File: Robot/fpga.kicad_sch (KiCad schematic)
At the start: 2 parts, among them U2 ICE40UP5K-SG48ITR, U3 74HCT245

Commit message: Update Robot SCH
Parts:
- added C1, C2: C, symbol Device:C
- added R1, R2, R3, R4: R, symbol Device:R
- added U4: DRV8845RHHR, symbol local:DRV8845
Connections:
- net GND: now also R1.1, R2.1, R3.1, R4.1, U4.16 (GND), U4.30 (PGND), U4.49 (PAD); no longer U3.13 (B5)
- net PWR_OFF: now also U2.10 (IOB_18a); no longer U2.42 (IOT_51a)
- net at U2.35 (IOT_46b_G0): now also U3.18 (B0); no longer U3.17 (B1)
- net at U2.36 (IOT_48b): now also U3.17 (B1); no longer U3.16 (B2)
- net at U2.37 (IOT_45a_G1): now also U4.11 (~{SLEEP}); no longer U3.18 (B0)
- net at U2.38 (IOT_50b): now also U3.15 (B3); no longer U3.14 (B4)
- net at U2.43 (IOT_49a): now also U3.16 (B2); no longer U3.15 (B3)
- net at U2.11 (IOB_20a): now also U3.13 (B5)
- net DLED: now reaches U3.7 (A5)
- net DRV_DIR1: no longer names the net of U2.25 (IOT_36b)
- net DRV_DIR1: now also U4.29 (I11), U4.34 (I01)
- net DRV_DIR2: no longer names the net of U2.23 (IOT_37a)
- net DRV_DIR2: now also U4.18 (PHASE1)
- net DRV_DIR3: no longer names the net of U2.27 (IOT_38b)
- net DRV_DIR3: now also U4.28 (I12), U4.35 (I02)
- net DRV_DIR4: no longer names the net of U2.26 (IOT_39a)
- net DRV_DIR4: now also U4.17 (PHASE2)
- net DRV_EN1: no longer names the net of U2.28 (IOT_41a)
- net DRV_EN1: now also U4.27 (I13), U4.36 (I03)
- net DRV_EN2: no longer names the net of U2.31 (IOT_42b)
- net DRV_EN2: now also U4.10 (PHASE3)
- net DRV_EN3: no longer names the net of U2.32 (IOT_43a)
- net DRV_EN3: now also U4.1 (I04), U4.19 (I14)
- net DRV_EN4: no longer names the net of U2.34 (IOT_44b)
- net DRV_EN4: now also U4.9 (PHASE4)
- new net: R2.2, U4.7 (SENSE2)
- new net: R1.2, U4.3 (SENSE1)
- new net: C2.1, U4.31 (VCP)
- new net: R4.2, U4.21 (SENSE4)
- new net: U2.42 (IOT_51a), U3.14 (B4)
- new net: R3.2, U4.25 (SENSE3)
- new net: C1.1, U4.32 (CP1)
- new net: C1.2, U4.33 (CP2)
- new net +12V: C2.2, U4.23 (VM2), U4.5 (VM1)
- new net VREF: U4.12 (VREF1), U4.13 (VREF2), U4.14 (VREF3), U4.15 (VREF4)
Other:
- moved on the sheet: U2A, U3

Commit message: Updated Robot SCH
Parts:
- removed unit 4 of U2
- added C3, C7, C8, C9: 1.0, symbol Device:C
- added C4, C5: 10n, symbol Device:C
- added C6: C_Polarized, symbol Device:C_Polarized
- added CN1, CN2, CN3, CN4: BM04B-SRSS-TB, easyeda2kicad:CONN-SMD_BM04B-SRSS-TB, symbol easyeda2kicad:BM04B-SRSS-TB
- added D1, D2, D3: KT-0603R, LED_SMD:LED_0603_1608Metric, symbol Device:LED
- added J3, J4, J5, J6: Motor, symbol Connector:Conn_01x02_Pin
- added R10, R11, R12, R13, R6, R7, R8, R9: NP, symbol Device:R
- added R14, R15, R16: R, symbol Device:R
- added SW2: User, symbol Switch:SW_Push
- C1: value C -> 22n
- C2: value C -> 0.22
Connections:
- net +12V: now also C4.2, C5.2, C6.1
- net +5V: now also C3.2
- net DLED: now also U3.9 (A7); no longer U3.7 (A5)
- net GND: now also U4.37 (PAD), C3.1, C4.1, C5.1, C6.2, C7.2, C8.2, C9.1, CN1.0, CN1.1, CN2.0, CN2.1, CN3.0, CN3.1, CN4.0, CN4.1, SW2.1; no longer U3.11 (B7), U3.12 (B6), U4.49 (PAD)
- net +3.3V: now reaches U2.33 (VCCIO_0)
- net +3.3V: now also U2.1 (VCCIO_2), U2.22 (SPI_VCCIO1), C7.1, C8.1, C9.2, CN1.4, CN2.4, CN3.4, CN4.4, R10.2, R11.2, R12.2, R13.2, R14.1, R15.1, R16.1, R6.2, R7.2, R8.2, R9.2
- net at U4.2 (OUT1A): now also J3.1 (Pin_1)
- net at U4.20 (OUT4A): now also J6.1 (Pin_1)
- net at U4.22 (OUT4B): now also J6.2 (Pin_2)
- net at U4.24 (OUT3B): now also J5.2 (Pin_2)
- net at U4.26 (OUT3A): now also J5.1 (Pin_1)
- net at U4.4 (OUT1B): now also J3.2 (Pin_2)
- net at U4.6 (OUT2B): now also J4.2 (Pin_2)
- net at U4.8 (OUT2A): now also J4.1 (Pin_1)
- net at U2.12 (IOB_22a): now also U3.12 (B6)
- net PwrBtnInput: now reaches U2.13 (IOB_24a)
- net at U2.20 (IOB_25b_G3): now also SW2.2
- net at U2.21 (IOB_23b): now also U3.11 (B7)
- net SERV7: now reaches U3.8 (A6)
- net DRV_QENCA1: no longer names the net of U2.46 (IOB_0a)
- net DRV_QENCA1: now also CN1.2, R11.1
- net DRV_QENCA2: no longer names the net of U2.47 (IOB_2a)
- net DRV_QENCA2: now also CN1.3, R10.1
- net DRV_QENCA3: no longer names the net of U2.44 (IOB_3b_G6)
- net DRV_QENCA3: now also CN2.2, R13.1
- net DRV_QENCA4: no longer names the net of U2.48 (IOB_4a)
- net DRV_QENCA4: now also CN2.3, R12.1
- net DRV_QENCB1: no longer names the net of U2.45 (IOB_5b)
- net DRV_QENCB1: now also CN3.2, R9.1
- net DRV_QENCB2: no longer names the net of U2.2 (IOB_6a)
- net DRV_QENCB2: now also CN3.3, R8.1
- net DRV_QENCB3: no longer names the net of U2.4 (IOB_8a)
- net DRV_QENCB3: now also CN4.2, R6.1
- net DRV_QENCB4: no longer names the net of U2.3 (IOB_9b)
- net DRV_QENCB4: now also CN4.3, R7.1
- net LED1: no longer names the net of U2.39 (RGB0)
- net LED1: now also D2.1 (K)
- net LED2: no longer names the net of U2.40 (RGB1)
- net LED2: now also D1.1 (K)
- net LED3: no longer names the net of U2.41 (RGB2)
- net LED3: now also D3.1 (K)
- net VREF renamed VREF ?
- new net: D2.2 (A), R14.2
- new net: D1.2 (A), R15.2
- new net: D3.2 (A), R16.2
- new net SERV6: U3.7 (A5)
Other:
- note added: "GND C1 C2 VCC"
- moved on the sheet: U2A, U2C

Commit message: Updated Robot SCH
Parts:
- removed CN1, CN2, CN3, CN4: BM04B-SRSS-TB, easyeda2kicad:CONN-SMD_BM04B-SRSS-TB, symbol easyeda2kicad:BM04B-SRSS-TB
- removed J3, J4, J5, J6: Motor, symbol Connector:Conn_01x02_Pin
- added C52: 1.0, symbol Device:C
- added J16: M1, symbol local:Motor
- added J17: M2, symbol local:Motor
- added J18: M3, symbol local:Motor
- added J19: M4, symbol local:Motor
- added R48, R49, R50, R51, R52, R53, R54, R55: 10K, symbol Device:R
- added U16: MCP4728, Package_SO:MSOP-10_3x3mm_P0.5mm, symbol Analog_DAC:MCP4728
- C6: value C_Polarized -> 470x16V
- R1, R2, R3, R4: value R -> FRM252WJR220TK (0.22); MPN (none) -> C7420023
- R14, R15, R16: value R -> ~
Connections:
- net +3.3V: now also C52.2, J16.2 (Vcc), J17.2 (Vcc), J18.2 (Vcc), J19.2 (Vcc), U16.1 (VDD)
- net GND: now also C52.1, J16.5 (GND), J17.5 (GND), J18.5 (GND), J19.5 (GND), R52.2, R53.2, R54.2, R55.2, U16.10 (VSS), U16.4 (~{LDAC})
- net SCL: now also U16.2 (SCL)
- net SDA: now also U16.3 (SDA)
- net at R11.1, U2.46 (IOB_0a): now also J16.4 (C1)
- net at R13.1, U2.44 (IOB_3b_G6): now also J17.4 (C1)
- net at R12.1, U2.48 (IOB_4a): now also J17.3 (C2)
- net at R8.1: now also U2.3 (IOB_9b), J19.3 (C2); no longer U2.2 (IOB_6a)
- net at R9.1: now also U2.4 (IOB_8a), J19.4 (C1); no longer U2.45 (IOB_5b)
- net at U4.8 (OUT2A): now also J17.6 (M+)
- net at U4.6 (OUT2B): now also J17.1 (M-)
- net at U4.26 (OUT3A): now also J18.6 (M+)
- net at U4.24 (OUT3B): now also J18.1 (M-)
- net at R6.1: now also U2.2 (IOB_6a), J18.3 (C2); no longer U2.4 (IOB_8a)
- net at R7.1: now also U2.45 (IOB_5b), J18.4 (C1); no longer U2.3 (IOB_9b)
- net at U4.2 (OUT1A): now also J16.6 (M+)
- net at U4.4 (OUT1B): now also J16.1 (M-)
- net at R10.1, U2.47 (IOB_2a): now also J16.3 (C2)
- net at U4.20 (OUT4A): now also J19.6 (M+)
- net at U4.22 (OUT4B): now also J19.1 (M-)
- removed net VREF ?: U4.12 (VREF1), U4.13 (VREF2), U4.14 (VREF3), U4.15 (VREF4)
- new net: R48.1, U16.6 (VOUTA)
- new net: R49.1, U16.7 (VOUTB)
- new net: R50.1, U16.8 (VOUTC)
- new net: R51.1, U16.9 (VOUTD)
- new net VREF1: R48.2, R52.1, U4.12 (VREF1)
- new net VREF2: R49.2, R53.1, U4.13 (VREF2)
- new net VREF3: R50.2, R54.1, U4.14 (VREF3)
- new net VREF4: R51.2, R55.1, U4.15 (VREF4)
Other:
- note removed: "GND C1 C2 VCC"

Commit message: Started PCB roughting
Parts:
- C10: renamed from C9; footprint (none) -> Capacitor_SMD:C_0603_1608Metric_Pad1.08x0.95mm_HandSolder
- C11: renamed from C52; footprint (none) -> Capacitor_SMD:C_0603_1608Metric_Pad1.08x0.95mm_HandSolder
- C2: renamed from C8; footprint (none) -> Capacitor_SMD:C_0603_1608Metric_Pad1.08x0.95mm_HandSolder
- C3: renamed from C6; footprint (none) -> Capacitor_THT:CP_Radial_D8.0mm_P3.80mm
- C4, C5: footprint (none) -> Capacitor_SMD:C_0603_1608Metric_Pad1.08x0.95mm_HandSolder
- C6: renamed from C1; footprint (none) -> Capacitor_SMD:C_0603_1608Metric_Pad1.08x0.95mm_HandSolder
- C7: renamed from C2; footprint (none) -> Capacitor_SMD:C_0603_1608Metric_Pad1.08x0.95mm_HandSolder
- C8: renamed from C7; footprint (none) -> Capacitor_SMD:C_0603_1608Metric_Pad1.08x0.95mm_HandSolder
- C9: renamed from C3; footprint (none) -> Capacitor_SMD:C_0603_1608Metric_Pad1.08x0.95mm_HandSolder
- J12: renamed from J16; footprint (none) -> easyeda2kicad:CONN-TH_S6B-XH-A-1-LF-SN
- J13: renamed from J17; footprint (none) -> easyeda2kicad:CONN-TH_S6B-XH-A-1-LF-SN
- J14: renamed from J18; footprint (none) -> easyeda2kicad:CONN-TH_S6B-XH-A-1-LF-SN
- J15: renamed from J19; footprint (none) -> easyeda2kicad:CONN-TH_S6B-XH-A-1-LF-SN
- R10: renamed from R16; footprint (none) -> Resistor_SMD:R_0603_1608Metric_Pad0.98x0.95mm_HandSolder
- R11: renamed from R12; footprint (none) -> Resistor_SMD:R_0603_1608Metric_Pad0.98x0.95mm_HandSolder
- R12: renamed from R13; footprint (none) -> Resistor_SMD:R_0603_1608Metric_Pad0.98x0.95mm_HandSolder
- R13: renamed from R10; footprint (none) -> Resistor_SMD:R_0603_1608Metric_Pad0.98x0.95mm_HandSolder
- R14: renamed from R11; footprint (none) -> Resistor_SMD:R_0603_1608Metric_Pad0.98x0.95mm_HandSolder
- R15: renamed from R7; footprint (none) -> Resistor_SMD:R_0603_1608Metric_Pad0.98x0.95mm_HandSolder
- R16: renamed from R6; footprint (none) -> Resistor_SMD:R_0603_1608Metric_Pad0.98x0.95mm_HandSolder
- R17: renamed from R9; footprint (none) -> Resistor_SMD:R_0603_1608Metric_Pad0.98x0.95mm_HandSolder
- R18: renamed from R8; footprint (none) -> Resistor_SMD:R_0603_1608Metric_Pad0.98x0.95mm_HandSolder
- R19: renamed from R48; footprint (none) -> Resistor_SMD:R_0603_1608Metric_Pad0.98x0.95mm_HandSolder
- R20: renamed from R52; footprint (none) -> Resistor_SMD:R_0603_1608Metric_Pad0.98x0.95mm_HandSolder
- R21: renamed from R49; footprint (none) -> Resistor_SMD:R_0603_1608Metric_Pad0.98x0.95mm_HandSolder
- R22: renamed from R53; footprint (none) -> Resistor_SMD:R_0603_1608Metric_Pad0.98x0.95mm_HandSolder
- R23: renamed from R50; footprint (none) -> Resistor_SMD:R_0603_1608Metric_Pad0.98x0.95mm_HandSolder
- R24: renamed from R54; footprint (none) -> Resistor_SMD:R_0603_1608Metric_Pad0.98x0.95mm_HandSolder
- R25: renamed from R51; footprint (none) -> Resistor_SMD:R_0603_1608Metric_Pad0.98x0.95mm_HandSolder
- R26: renamed from R55; footprint (none) -> Resistor_SMD:R_0603_1608Metric_Pad0.98x0.95mm_HandSolder
- R4: renamed from R1; footprint (none) -> Resistor_SMD:R_2512_6332Metric_Pad1.40x3.35mm_HandSolder
- R5: renamed from R2; footprint (none) -> Resistor_SMD:R_2512_6332Metric_Pad1.40x3.35mm_HandSolder
- R6: renamed from R3; footprint (none) -> Resistor_SMD:R_2512_6332Metric_Pad1.40x3.35mm_HandSolder
- R7: renamed from R4; footprint (none) -> Resistor_SMD:R_2512_6332Metric_Pad1.40x3.35mm_HandSolder
- R8: renamed from R14; footprint (none) -> Resistor_SMD:R_0603_1608Metric_Pad0.98x0.95mm_HandSolder
- R9: renamed from R15; footprint (none) -> Resistor_SMD:R_0603_1608Metric_Pad0.98x0.95mm_HandSolder
- SW1: renamed from SW2; footprint (none) -> locals:KEY-TH_2P-L6.0-W3.5-P6.50
- U3: renamed from U4; footprint (none) -> easyeda2kicad:VQFN-36_L6.0-W6.0-P0.50-TL-EP4.1
- U5: renamed from U3; footprint (none) -> easyeda2kicad:TSSOP-20_L6.5-W4.4-P0.65-LS6.4-BL
- renumbered D2 to D1, D1 to D2, U2 to U4, U16 to U6
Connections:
- net VREF1: now also R25.2, R26.1; no longer R19.2, R20.1
- net VREF2: now also R23.2, R24.1; no longer R21.2, R22.1
- net VREF3: now also R21.2, R22.1; no longer R23.2, R24.1
- net VREF4: now also R19.2, R20.1; no longer R25.2, R26.1

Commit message: Updated PCB & Patterns for Robot
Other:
- company: (none) -> RoboWay
- title: (none) -> FPGA
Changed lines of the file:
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@@
 	(generator_version "9.0")
 	(paper "A4")
+	(title_block
+		(title "FPGA")
+		(company "RoboWay")
+	)
 	(junction
 		(at 96.52 63.5)

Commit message: Updated PCB for Robot (routing in progress)
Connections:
- net +3.3V: now also D1.2 (A), D2.2 (A), D3.2 (A); no longer R10.1, R8.1, R9.1
- net at D1.1 (K): now also R8.1; no longer U4.39 (RGB0)
- net at R8.2: now also U4.39 (RGB0); no longer D1.2 (A)
- net at D2.1 (K): now also R9.1; no longer U4.40 (RGB1)
- net at R9.2: now also U4.40 (RGB1); no longer D2.2 (A)
- net at U4.41 (RGB2): now also R10.2; no longer D3.1 (K)
- new net: D3.1 (K), R10.1
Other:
- moved on the sheet: D3
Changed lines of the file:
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@@
 	(symbol
 		(lib_id "Device:LED")
-		(at 203.2 81.28 180)
+		(at 187.96 81.28 180)
 		(unit 1)
 		(exclude_from_sim no)
@@
 		(fields_autoplaced yes)
 		(property "Reference" "D1"
-			(at 204.7875 73.66 0)
+			(at 189.5475 73.66 0)
 			(effects
 				(font
@@
 		)
 		(property "Value" "KT-0603R"
-			(at 204.7875 76.2 0)
+			(at 189.5475 76.2 0)
 			(effects
 				(font
@@
 		)
 		(property "Footprint" "LED_SMD:LED_0603_1608Metric"
-			(at 203.2 81.28 0)
+			(at 187.96 81.28 0)
 			(effects
 				(font
@@
 		)
 		(property "Datasheet" "~"
-			(at 203.2 81.28 0)
+			(at 187.96 81.28 0)
 			(effects
 				(font
@@
 		)
 		(property "Description" ""
-			(at 203.2 81.28 0)
+			(at 187.96 81.28 0)
 			(effects
 				(font
@@
 		)
 		(property "MPN" "C2286"
-			(at 203.2 81.28 0)
+			(at 187.96 81.28 0)
 			(effects
 				(font
@@
 	(symbol
 		(lib_id "Device:LED")
-		(at 203.2 83.82 180)
+		(at 187.96 83.82 180)
 		(unit 1)
 		(exclude_from_sim no)
@@
 		(fields_autoplaced yes)
 		(property "Reference" "D2"
-			(at 204.7875 76.2 0)
+			(at 189.5475 76.2 0)
 			(effects
 				(font
@@
 		)
 		(property "Value" "KT-0603R"
-			(at 204.7875 78.74 0)
+			(at 189.5475 78.74 0)
 			(effects
 				(font
@@
 		)
 		(property "Footprint" "LED_SMD:LED_0603_1608Metric"
-			(at 203.2 83.82 0)
+			(at 187.96 83.82 0)
 			(effects
 				(font
@@
 		)
 		(property "Datasheet" "~"
-			(at 203.2 83.82 0)
+			(at 187.96 83.82 0)
 			(effects
 				(font
@@
 		)
 		(property "Description" ""
-			(at 203.2 83.82 0)
+			(at 187.96 83.82 0)
 			(effects
 				(font
@@
 		)
 		(property "MPN" "C2286"
-			(at 203.2 83.82 0)
+			(at 187.96 83.82 0)
 			(effects
 				(font
@@
 	(symbol
 		(lib_id "Device:R")
-		(at 187.96 83.82 90)
+		(at 203.2 83.82 90)
 		(unit 1)
 		(exclude_from_sim no)
@@
 		(fields_autoplaced yes)
 		(property "Reference" "R9"
-			(at 187.96 77.47 90)
+			(at 203.2 77.47 90)
 			(effects
 				(font
@@
 		)
 		(property "Value" "~"
-			(at 187.96 80.01 90)
+			(at 203.2 80.01 90)
 			(effects
 				(font
@@
 		)
 		(property "Footprint" "Resistor_SMD:R_0603_1608Metric_Pad0.98x0.95mm_HandSolder"
-			(at 187.96 85.598 90)
+			(at 203.2 85.598 90)
 			(effects
 				(font
@@
 		)
 		(property "Datasheet" "~"
-			(at 187.96 83.82 0)
+			(at 203.2 83.82 0)
 			(effects
 				(font
@@
 		)
 		(property "Description" "Resistor"
-			(at 187.96 83.82 0)
+			(at 203.2 83.82 0)
 			(effects
 				(font
@@
 	(symbol
 		(lib_id "Device:LED")
-		(at 203.2 86.36 180)
+		(at 187.96 86.36 180)
 		(unit 1)
 		(exclude_from_sim no)
@@
 		(dnp no)
 		(property "Reference" "D3"
-			(at 200.152 88.9 0)
+			(at 184.912 88.9 0)
 			(effects
 				(font
@@
 		)
 		(property "Value" "KT-0603R"
-			(at 207.264 88.9 0)
+			(at 192.024 88.9 0)
 			(effects
 				(font
@@
 		)
 		(property "Footprint" "LED_SMD:LED_0603_1608Metric"
-			(at 203.2 86.36 0)
+			(at 187.96 86.36 0)
 			(effects
 				(font
@@
 		)
 		(property "Datasheet" "~"
-			(at 203.2 86.36 0)
+			(at 187.96 86.36 0)
 			(effects
 				(font
@@
 		)
 		(property "Description" ""
-			(at 203.2 86.36 0)
+			(at 187.96 86.36 0)
 			(effects
 				(font
@@
 		)
 		(property "MPN" "C2286"
-			(at 203.2 86.36 0)
+			(at 187.96 86.36 0)
 			(effects
 				(font
@@
 	(symbol
 		(lib_id "Device:R")
-		(at 187.96 86.36 90)
+		(at 203.2 86.36 90)
 		(unit 1)
 		(exclude_from_sim no)
@@
 		(fields_autoplaced yes)
 		(property "Reference" "R10"
-			(at 187.96 80.01 90)
+			(at 203.2 80.01 90)
 			(effects
 				(font
@@
 		)
 		(property "Value" "~"
-			(at 187.96 82.55 90)
+			(at 203.2 82.55 90)
 			(effects
 				(font
@@
 		)
 		(property "Footprint" "Resistor_SMD:R_0603_1608Metric_Pad0.98x0.95mm_HandSolder"
-			(at 187.96 88.138 90)
+			(at 203.2 88.138 90)
 			(effects
 				(font
@@
 		)
 		(property "Datasheet" "~"
-			(at 187.96 86.36 0)
+			(at 203.2 86.36 0)
 			(effects
 				(font
@@
 		)
 		(property "Description" "Resistor"
-			(at 187.96 86.36 0)
+			(at 203.2 86.36 0)
 			(effects
 				(font
@@
 	(symbol
 		(lib_id "Device:R")
-		(at 187.96 81.28 90)
+		(at 203.2 81.28 90)
 		(unit 1)
 		(exclude_from_sim no)
@@
 		(fields_autoplaced yes)
 		(property "Reference" "R8"
-			(at 187.96 74.93 90)
+			(at 203.2 74.93 90)
 			(effects
 				(font
@@
 		)
 		(property "Value" "~"
-			(at 187.96 77.47 90)
+			(at 203.2 77.47 90)
 			(effects
 				(font
@@
 		)
 		(property "Footprint" "Resistor_SMD:R_0603_1608Metric_Pad0.98x0.95mm_HandSolder"
-			(at 187.96 83.058 90)
+			(at 203.2 83.058 90)
 			(effects
 				(font
@@
 		)
 		(property "Datasheet" "~"
-			(at 187.96 81.28 0)
+			(at 203.2 81.28 0)
 			(effects
 				(font
@@
 		)
 		(property "Description" "Resistor"
-			(at 187.96 81.28 0)
+			(at 203.2 81.28 0)
 			(effects
 				(font

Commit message: Updated PCB for Robot (routing in progress)
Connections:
- net +3.3V renamed +3V3
- no-connect marks 0 -> 1

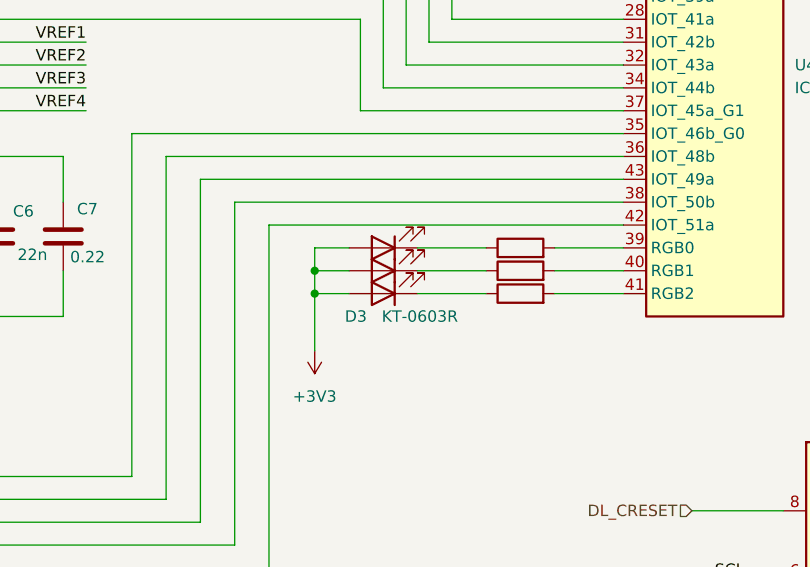
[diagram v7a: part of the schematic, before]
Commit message: Updated PCB for Robot (routing close to finish)
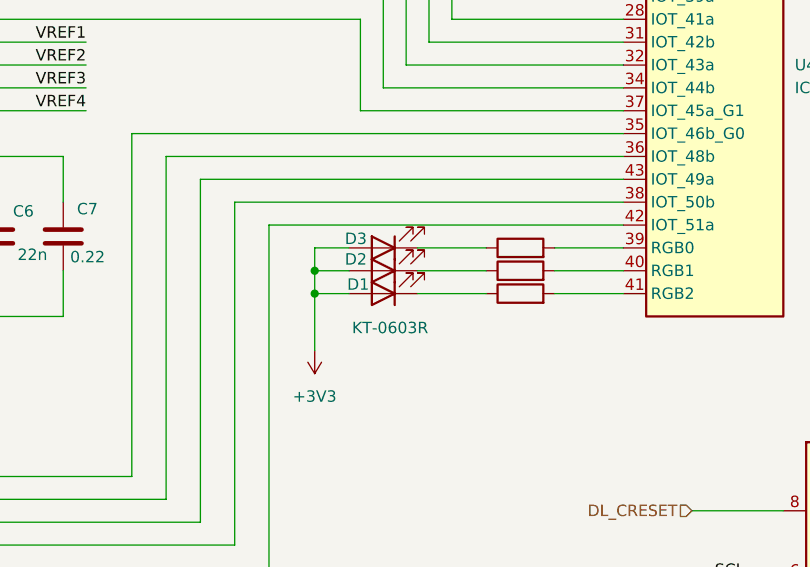
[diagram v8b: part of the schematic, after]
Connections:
- net at U4.39 (RGB0): now also R10.2; no longer R8.2
- net at U4.41 (RGB2): now also R8.2; no longer R10.2
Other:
- moved on the sheet: D3
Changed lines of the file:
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@@
 	(wire
 		(pts
-			(xy 191.77 81.28) (xy 199.39 81.28)
+			(xy 191.77 86.36) (xy 199.39 86.36)
 		)
 		(stroke
@@
 	(wire
 		(pts
-			(xy 191.77 86.36) (xy 199.39 86.36)
+			(xy 191.77 81.28) (xy 199.39 81.28)
 		)
 		(stroke
@@
 	(symbol
 		(lib_id "Device:LED")
-		(at 187.96 81.28 180)
+		(at 187.96 86.36 180)
 		(unit 1)
 		(exclude_from_sim no)
@@
 		(on_board yes)
 		(dnp no)
-		(fields_autoplaced yes)
 		(property "Reference" "D1"
-			(at 189.5475 73.66 0)
+			(at 185.166 85.344 0)
 			(effects
 				(font
 					(size 1.27 1.27)
 				)
-				(hide yes)
 			)
 		)
 		(property "Value" "KT-0603R"
-			(at 189.5475 76.2 0)
+			(at 188.722 90.17 0)
 			(effects
 				(font
 					(size 1.27 1.27)
 				)
-				(hide yes)
 			)
 		)
 		(property "Footprint" "LED_SMD:LED_0603_1608Metric"
-			(at 187.96 81.28 0)
+			(at 187.96 86.36 0)
 			(effects
 				(font
@@
 		)
 		(property "Datasheet" "~"
-			(at 187.96 81.28 0)
+			(at 187.96 86.36 0)
 			(effects
 				(font
@@
 		)
 		(property "Description" ""
-			(at 187.96 81.28 0)
+			(at 187.96 86.36 0)
 			(effects
 				(font
@@
 		)
 		(property "MPN" "C2286"
-			(at 187.96 81.28 0)
+			(at 187.96 86.36 0)
 			(effects
 				(font
@@
 		(on_board yes)
 		(dnp no)
-		(fields_autoplaced yes)
 		(property "Reference" "D2"
-			(at 189.5475 76.2 0)
+			(at 184.912 82.55 0)
 			(effects
 				(font
 					(size 1.27 1.27)
 				)
-				(hide yes)
 			)
 		)
@@
 	(symbol
 		(lib_id "Device:LED")
-		(at 187.96 86.36 180)
+		(at 187.96 81.28 180)
 		(unit 1)
 		(exclude_from_sim no)
@@
 		(dnp no)
 		(property "Reference" "D3"
-			(at 184.912 88.9 0)
+			(at 184.912 80.264 0)
 			(effects
 				(font
@@
 		)
 		(property "Value" "KT-0603R"
-			(at 192.024 88.9 0)
+			(at 192.024 83.82 0)
 			(effects
 				(font
 					(size 1.27 1.27)
 				)
+				(hide yes)
 			)
 		)
 		(property "Footprint" "LED_SMD:LED_0603_1608Metric"
-			(at 187.96 86.36 0)
+			(at 187.96 81.28 0)
 			(effects
 				(font
@@
 		)
 		(property "Datasheet" "~"
-			(at 187.96 86.36 0)
+			(at 187.96 81.28 0)
 			(effects
 				(font
@@
 		)
 		(property "Description" ""
-			(at 187.96 86.36 0)
+			(at 187.96 81.28 0)
 			(effects
 				(font
@@
 		)
 		(property "MPN" "C2286"
-			(at 187.96 86.36 0)
+			(at 187.96 81.28 0)
 			(effects
 				(font
@@
 	(symbol
 		(lib_id "Device:R")
-		(at 203.2 86.36 90)
+		(at 203.2 81.28 90)
 		(unit 1)
 		(exclude_from_sim no)
@@
 		(fields_autoplaced yes)
 		(property "Reference" "R10"
-			(at 203.2 80.01 90)
+			(at 203.2 74.93 90)
 			(effects
 				(font
@@
 		)
 		(property "Value" "~"
-			(at 203.2 82.55 90)
+			(at 203.2 77.47 90)
 			(effects
 				(font
@@
 		)
 		(property "Footprint" "Resistor_SMD:R_0603_1608Metric_Pad0.98x0.95mm_HandSolder"
-			(at 203.2 88.138 90)
+			(at 203.2 83.058 90)
 			(effects
 				(font
@@
 		)
 		(property "Datasheet" "~"
-			(at 203.2 86.36 0)
+			(at 203.2 81.28 0)
 			(effects
 				(font
@@
 		)
 		(property "Description" "Resistor"
-			(at 203.2 86.36 0)
+			(at 203.2 81.28 0)
 			(effects
 				(font
@@
 	(symbol
 		(lib_id "Device:R")
-		(at 203.2 81.28 90)
+		(at 203.2 86.36 90)
 		(unit 1)
 		(exclude_from_sim no)
@@
 		(fields_autoplaced yes)
 		(property "Reference" "R8"
-			(at 203.2 74.93 90)
+			(at 203.2 80.01 90)
 			(effects
 				(font
@@
 		)
 		(property "Value" "~"
-			(at 203.2 77.47 90)
+			(at 203.2 82.55 90)
 			(effects
 				(font
@@
 		)
 		(property "Footprint" "Resistor_SMD:R_0603_1608Metric_Pad0.98x0.95mm_HandSolder"
-			(at 203.2 83.058 90)
+			(at 203.2 88.138 90)
 			(effects
 				(font
@@
 		)
 		(property "Datasheet" "~"
-			(at 203.2 81.28 0)
+			(at 203.2 86.36 0)
 			(effects
 				(font
@@
 		)
 		(property "Description" "Resistor"
-			(at 203.2 81.28 0)
+			(at 203.2 86.36 0)
 			(effects
 				(font
